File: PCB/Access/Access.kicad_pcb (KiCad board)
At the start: 2 copper layers, 70 x 70 mm, 85 parts, among them J1 USB-C, J2 RFID, J3 INPUTS, J4 USB-PROG, J5 POWER, J6 DOOR2, J7 DOOR1, J8 Shelly, Q2 PMF250XNEX, SW1 ESE13V01A, U1 MD8942, U10 ESP32-S3-MINI-1, U2 MD8942, U3 G3VM-41GR8, U8 G3VM-41GR8

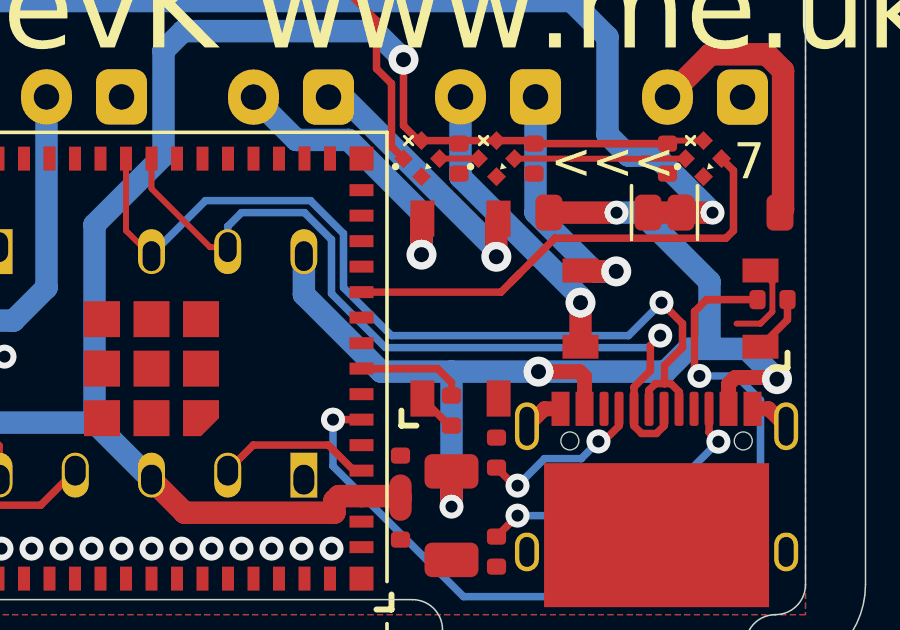
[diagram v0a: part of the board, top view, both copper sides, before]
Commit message: Clear to avoid solder draining down hole instead of pad
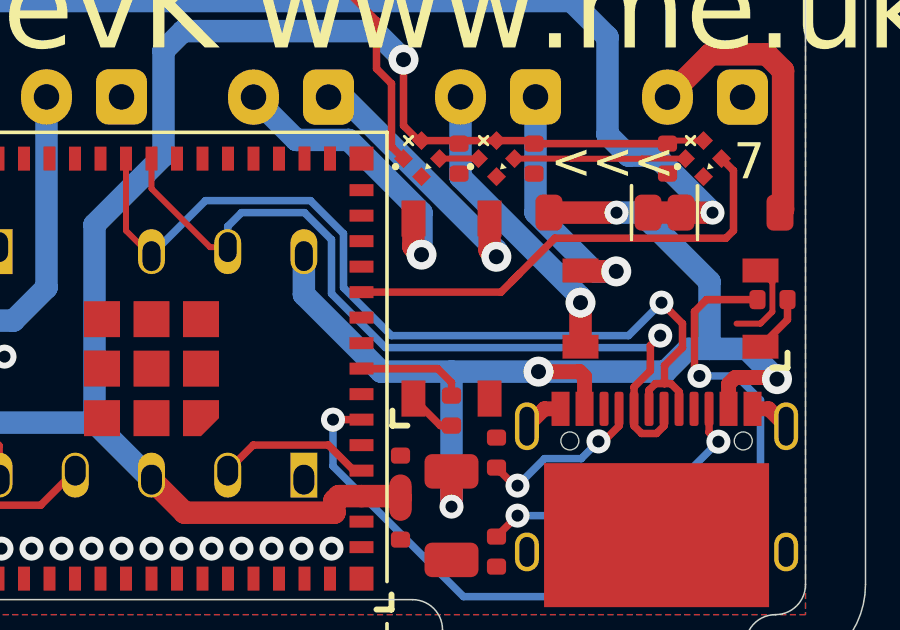
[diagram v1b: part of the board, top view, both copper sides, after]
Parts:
- moved U3 0.30 mm to (113.0, 101.5)

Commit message: Library update
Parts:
- moved D1 0.23 mm to (90.5, 98.5)
- moved D2 0.23 mm to (87.9, 98.5)
- moved D3 0.23 mm to (85.4, 98.5)
- moved D4 0.23 mm to (82.9, 98.5)
- moved D6 0.22 mm to (80.4, 98.5)
- moved D8 0.22 mm to (77.9, 98.5)
- moved D10 0.10 mm to (93.8, 96.4)
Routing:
- net GND: track 5.62 -> 20.2 mm, vias 82 -> 81
- net Net-(J3-Pin_1): track 6.90 -> 8.11 mm

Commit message: Library update
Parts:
- C1, C21: value 10uF 50V -> 10uF 35V

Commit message: Tidy
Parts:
- moved J1 1.39 mm to (119.8, 105.9)
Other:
- copper layers 2 -> 4
- board text removed: "15"
- board text removed: "16"
- board text removed: "17"
- board text removed: "18"
- board text removed: "19"
- board text removed: "21"
- board text removed: "22"
- board text removed: "23"
